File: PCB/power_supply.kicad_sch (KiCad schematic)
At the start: 7 parts, among them SW1 SW_MEC_5G

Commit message: add footprints for power supply
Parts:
- C1: footprint Capacitor_SMD:CP_Elec_6.3x7.7 -> Capacitor_SMD:CP_Elec_6.3x5.4
- D12: footprint Capacitor_SMD:C_0805_2012Metric -> Diode_SMD:D_SMA; link (none) -> https://www.tme.eu/de/details/ss14-dc/schottkydioden-smd/dc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
- L1: footprint Inductor_SMD:L_APV_APH0650 -> Inductor_SMD:L_Bourns-SRN6028; link (none) -> https://www.tme.eu/de/details/djnr6028-470-s/drosseln/ferro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
- SW1: footprint Button_Switch_THT:SW_NKK_GW12LJP -> Button_Switch_SMD:SW_Tactile_SPST_NO_Straight_CK_PTS636Sx25SMTRLFS
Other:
- note added: "Ask Jule, what battery cell holder???"
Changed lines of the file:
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@@
 	(generator_version "10.0")
 	(paper "A4")
+	(text "Ask Jule, what battery cell holder???\n"
+		(exclude_from_sim no)
+		(at 77.47 70.358 0)
+		(effects
+			(font
+				(size 1.27 1.27)
+			)
+		)
+	)
 	(text "Power Supply"
 		(exclude_from_sim no)
-		(at 156.718 59.182 0)
+		(at 162.56 55.372 0)
 		(effects
 			(font
@@
 			(width 0)
 			(type default)
-		)
-	)
-	(label "5v"
-		(at 196.85 78.74 0)
-		(effects
-			(font
-				(size 1.27 1.27)
-			)
-			(justify left bottom)
 		)
 	)
@@
 			)
 		)
-		(property "Footprint" "Capacitor_SMD:C_0805_2012Metric"
+		(property "Footprint" "Diode_SMD:D_SMA"
 			(at 158.75 95.25 0)
 			(hide yes)
@@
 		)
 		(property "Description" "Schottky diode"
+			(at 158.75 95.25 0)
+			(hide yes)
+			(show_name no)
+			(do_not_autoplace no)
+			(effects
+				(font
+					(size 1.27 1.27)
+				)
+			)
+		)
+		(property "link" "https://www.tme.eu/de/details/ss14-dc/schottkydioden-smd/dc-components/ss14/"
 			(at 158.75 95.25 0)
 			(hide yes)
@@
 			)
 		)
-		(property "Footprint" "Inductor_SMD:L_APV_APH0650"
+		(property "Footprint" "Inductor_SMD:L_Bourns-SRN6028"
 			(at 167.64 68.58 0)
 			(hide yes)
@@
 		(property "Description" "Inductor"
 			(at 167.64 68.58 0)
+			(hide yes)
+			(show_name no)
+			(do_not_autoplace no)
+			(effects
+				(font
+					(size 1.27 1.27)
+				)
+			)
+		)
+		(property "link" "https://www.tme.eu/de/details/djnr6028-470-s/drosseln/ferrocore/"
+			(at 167.64 68.58 90)
 			(hide yes)
 			(show_name no)
@@
 			)
 		)
-		(property "Datasheet" ""
+		(property "Datasheet" "https://de.aliexpress.com/item/1005009130833374.html?spm=a2g0o.order_list.order_list_main.5.39695c5fGREGny&gatewayAdapt=glo2deu"
 			(at 167.64 81.28 0)
 			(hide yes)
@@
 			)
 		)
-		(property "Footprint" "Button_Switch_THT:SW_NKK_GW12LJP"
+		(property "Footprint" "Button_Switch_SMD:SW_Tactile_SPST_NO_Straight_CK_PTS636Sx25SMTRLFS"
 			(at 133.35 63.5 0)
 			(hide yes)
@@
 			)
 		)
-		(property "Description" "MEC 5G single pole normally-open tactile switch"
+		(property "Description" "https://www.tme.eu/de/details/tact4203-319160-r/mikroschalter-tact/connfly/ds1042-03-319kkr16010/"
+			(at 133.35 68.58 0)
+			(hide yes)
+			(show_name no)
+			(do_not_autoplace no)
+			(effects
+				(font
+					(size 1.27 1.27)
+				)
+			)
+		)
+		(property "Field5" ""
 			(at 133.35 68.58 0)
 			(hide yes)
@@
 			)
 		)
-		(property "Footprint" "Capacitor_SMD:CP_Elec_6.3x7.7"
+		(property "Footprint" "Capacitor_SMD:CP_Elec_6.3x5.4"
 			(at 117.8052 81.28 0)
 			(hide yes)
@@
 			)
 		)
-		(property "Description" "Polarized capacitor"
+		(property "Description" "https://www.tme.eu/de/details/vs0j221me054000ce0/elektrolytische-kondensatoren-smd/chang/"
 			(at 116.84 77.47 0)
 			(hide yes)

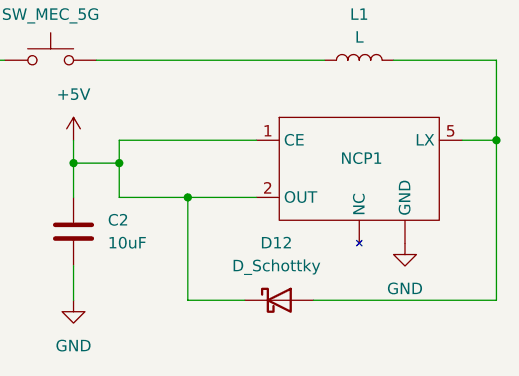
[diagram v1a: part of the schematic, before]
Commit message: update LED footprint reverse mount
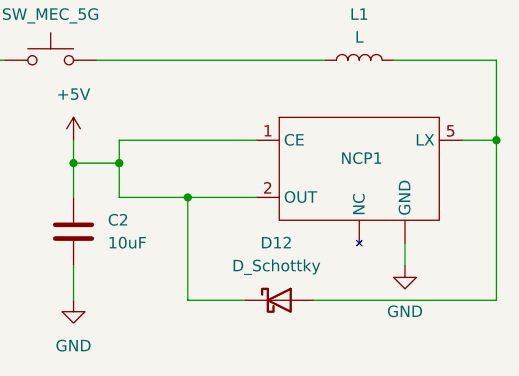
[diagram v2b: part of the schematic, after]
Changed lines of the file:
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@@
+	(wire
+		(pts
+			(xy 172.72 91.44) (xy 172.72 88.9)
+		)
+		(stroke
+			(width 0)
+			(type default)
+		)
+	)
 	(wire
 		(pts
@@
 	(symbol
 		(lib_id "power:GND")
-		(at 172.72 88.9 0)
+		(at 172.72 91.44 0)
 		(unit 1)
 		(body_style 1)
@@
 		(fields_autoplaced yes)
 		(property "Reference" "#PWR04"
-			(at 172.72 95.25 0)
+			(at 172.72 97.79 0)
 			(hide yes)
 			(show_name no)
@@
 		)
 		(property "Value" "GND"
-			(at 172.72 93.98 0)
+			(at 172.72 96.52 0)
 			(show_name no)
 			(do_not_autoplace no)
@@
 		)
 		(property "Footprint" ""
-			(at 172.72 88.9 0)
+			(at 172.72 91.44 0)
 			(hide yes)
 			(show_name no)
@@
 		)
 		(property "Datasheet" ""
-			(at 172.72 88.9 0)
+			(at 172.72 91.44 0)
 			(hide yes)
 			(show_name no)
@@
 		)
 		(property "Description" "Power symbol creates a global label with name \"GND\" , ground"
-			(at 172.72 88.9 0)
+			(at 172.72 91.44 0)
 			(hide yes)
 			(show_name no)

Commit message: component distributions
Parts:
- removed SW1: SW_MEC_5G, Button_Switch_SMD:SW_Tactile_SPST_NO_Straight_CK_PTS636Sx25SMTRLFS, symbol Switch:SW_MEC_5G
- added SW3, SW4: SW_Push, Button_Switch_SMD:SW_Push_1P1T_NO_CK_PTS125Sx73PSMTR, symbol Switch:SW_Push
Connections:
- net +3.3V: now also SW3.1, SW4.1
- net GND: now also NCP1.4 (GND); no longer NCP1. (GND)
- net at L1.1: now also SW3.2, SW4.2
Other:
- moved on the sheet: D12
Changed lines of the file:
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@@
+	)
+	(junction
+		(at 142.24 68.58)
+		(diameter 0)
+		(color 0 0 0 0)
 	)
 	(junction
@@
 	)
 	(junction
+		(at 124.46 68.58)
+		(diameter 0)
+		(color 0 0 0 0)
+	)
+	(junction
 		(at 140.97 80.01)
 		(diameter 0)
@@
 	(wire
 		(pts
+			(xy 128.27 53.34) (xy 124.46 53.34)
+		)
+		(stroke
+			(width 0)
+			(type default)
+		)
+	)
+	(wire
+		(pts
+			(xy 142.24 53.34) (xy 142.24 68.58)
+		)
+		(stroke
+			(width 0)
+			(type default)
+		)
+	)
+	(wire
+		(pts
 			(xy 135.89 83.82) (xy 135.89 80.01)
 		)
@@
 	(wire
 		(pts
-			(xy 148.59 95.25) (xy 148.59 83.82)
+			(xy 148.59 100.33) (xy 148.59 83.82)
+		)
+		(stroke
+			(width 0)
+			(type default)
+		)
+	)
+	(wire
+		(pts
+			(xy 124.46 68.58) (xy 116.84 68.58)
 		)
 		(stroke
@@
 	(wire
 		(pts
+			(xy 124.46 53.34) (xy 124.46 68.58)
+		)
+		(stroke
+			(width 0)
+			(type default)
+		)
+	)
+	(wire
+		(pts
 			(xy 182.88 77.47) (xy 179.07 77.47)
 		)
@@
 	(wire
 		(pts
-			(xy 182.88 77.47) (xy 182.88 95.25)
+			(xy 182.88 77.47) (xy 182.88 100.33)
 		)
 		(stroke
@@
 	(wire
 		(pts
-			(xy 138.43 68.58) (xy 163.83 68.58)
+			(xy 138.43 68.58) (xy 142.24 68.58)
 		)
 		(stroke
@@
 	(wire
 		(pts
-			(xy 154.94 95.25) (xy 148.59 95.25)
+			(xy 154.94 100.33) (xy 148.59 100.33)
 		)
 		(stroke
@@
 	(wire
 		(pts
-			(xy 162.56 95.25) (xy 182.88 95.25)
-		)
-		(stroke
-			(width 0)
-			(type default)
-		)
-	)
-	(wire
-		(pts
-			(xy 128.27 68.58) (xy 116.84 68.58)
+			(xy 162.56 100.33) (xy 182.88 100.33)
+		)
+		(stroke
+			(width 0)
+			(type default)
+		)
+	)
+	(wire
+		(pts
+			(xy 128.27 68.58) (xy 124.46 68.58)
+		)
+		(stroke
+			(width 0)
+			(type default)
+		)
+	)
+	(wire
+		(pts
+			(xy 142.24 68.58) (xy 163.83 68.58)
 		)
 		(stroke
@@
 		(pts
 			(xy 105.41 68.58) (xy 105.41 73.66)
+		)
+		(stroke
+			(width 0)
+			(type default)
+		)
+	)
+	(wire
+		(pts
+			(xy 138.43 53.34) (xy 142.24 53.34)
 		)
 		(stroke
@@
 	(symbol
 		(lib_id "Device:D_Schottky")
-		(at 158.75 95.25 0)
+		(at 158.75 100.33 0)
 		(unit 1)
 		(body_style 1)
@@
 		(fields_autoplaced yes)
 		(property "Reference" "D12"
-			(at 158.4325 88.9 0)
+			(at 158.4325 93.98 0)
 			(show_name no)
 			(do_not_autoplace no)
@@
 		)
 		(property "Value" "D_Schottky"
-			(at 158.4325 91.44 0)
+			(at 158.4325 96.52 0)
 			(show_name no)
 			(do_not_autoplace no)
@@
 		)
 		(property "Footprint" "Diode_SMD:D_SMA"
-			(at 158.75 95.25 0)
+			(at 158.75 100.33 0)
 			(hide yes)
 			(show_name no)
@@
 		)
 		(property "Datasheet" ""
-			(at 158.75 95.25 0)
+			(at 158.75 100.33 0)
 			(hide yes)
 			(show_name no)
@@
 		)
 		(property "Description" "Schottky diode"
-			(at 158.75 95.25 0)
+			(at 158.75 100.33 0)
 			(hide yes)
 			(show_name no)
@@
 		)
 		(property "link" "https://www.tme.eu/de/details/ss14-dc/schottkydioden-smd/dc-components/ss14/"
-			(at 158.75 95.25 0)
+			(at 158.75 100.33 0)
 			(hide yes)
 			(show_name no)
@@
 				(path "/510c3167-274e-48e8-bc0f-ce517acc7f9d/31fe11dc-c780-463d-b2c9-9ca8c0ac4f4e"
 					(reference "BT1")
+					(unit 1)
+				)
+			)
+		)
+	)
+	(symbol
+		(lib_id "Switch:SW_Push")
+		(at 133.35 68.58 0)
+		(unit 1)
+		(body_style 1)
+		(exclude_from_sim no)
+		(in_bom yes)
+		(on_board yes)
+		(in_pos_files yes)
+		(dnp no)
+		(fields_autoplaced yes)
+		(property "Reference" "SW4"
+			(at 133.35 60.96 0)
+			(show_name no)
+			(do_not_autoplace no)
+			(effects
+				(font
+					(size 1.27 1.27)
+				)
+			)
+		)
+		(property "Value" "SW_Push"
+			(at 133.35 63.5 0)
+			(show_name no)
+			(do_not_autoplace no)
+			(effects
+				(font
+					(size 1.27 1.27)
+				)
+			)
+		)
+		(property "Footprint" "Button_Switch_SMD:SW_Push_1P1T_NO_CK_PTS125Sx73PSMTR"
+			(at 133.35 63.5 0)
+			(hide yes)
+			(show_name no)
+			(do_not_autoplace no)
+			(effects
+				(font
+					(size 1.27 1.27)
+				)
+			)
+		)
+		(property "Datasheet" "https://www.apem.com/medias/download/MEC_switches_serie_MULTIMEC5G.pdf"
+			(at 133.35 63.5 0)
+			(hide yes)
+			(show_name no)
+			(do_not_autoplace no)
+			(effects
+				(font
+					(size 1.27 1.27)
+				)
+			)
+		)
+		(property "Description" "Push button switch, generic, two pins"
+			(at 133.35 68.58 0)
+			(hide yes)
+			(show_name no)
+			(do_not_autoplace no)
+			(effects
+				(font
+					(size 1.27 1.27)
+				)
+			)
+		)
+		(pin "1"
+		)
+		(pin "2"
+		)
+		(instances
+			(project "UV_badge"
+				(path "/510c3167-274e-48e8-bc0f-ce517acc7f9d/31fe11dc-c780-463d-b2c9-9ca8c0ac4f4e"
+					(reference "SW4")
 					(unit 1)
 				)
@@
 	)
 	(symbol
+		(lib_id "Switch:SW_Push")
+		(at 133.35 53.34 0)
+		(unit 1)
+		(body_style 1)
+		(exclude_from_sim no)
+		(in_bom yes)
+		(on_board yes)
+		(in_pos_files yes)
+		(dnp no)
+		(fields_autoplaced yes)
+		(property "Reference" "SW3"
+			(at 133.35 45.72 0)
+			(show_name no)
+			(do_not_autoplace no)
+			(effects
+				(font
+					(size 1.27 1.27)
+				)
+			)
+		)
+		(property "Value" "SW_Push"
+			(at 133.35 48.26 0)
+			(show_name no)
+			(do_not_autoplace no)
+			(effects
+				(font
+					(size 1.27 1.27)
+				)
+			)
+		)
+		(property "Footprint" "Button_Switch_SMD:SW_Push_1P1T_NO_CK_PTS125Sx73PSMTR"
+			(at 133.35 48.26 0)
+			(hide yes)
+			(show_name no)
+			(do_not_autoplace no)
+			(effects
+				(font
+					(size 1.27 1.27)
+				)
+			)
+		)
+		(property "Datasheet" "https://www.apem.com/medias/download/MEC_switches_serie_MULTIMEC5G.pdf"
+			(at 133.35 48.26 0)
+			(hide yes)
+			(show_name no)
+			(do_not_autoplace no)
+			(effects
+				(font
+					(size 1.27 1.27)
+				)
+			)
+		)
+		(property "Description" "Push button switch, generic, two pins"
+			(at 133.35 53.34 0)
+			(hide yes)
+			(show_name no)
+			(do_not_autoplace no)
+			(effects
+				(font
+					(size 1.27 1.27)
+				)
+			)
+		)
+		(pin "1"
+		)
+		(pin "2"
+		)
+		(instances
+			(project "UV_badge"
+				(path "/510c3167-274e-48e8-bc0f-ce517acc7f9d/31fe11dc-c780-463d-b2c9-9ca8c0ac4f4e"
+					(reference "SW3")
+					(unit 1)
+				)
+			)
+		)
+	)
+	(symbol
 		(lib_id "custom:NCP1402")
 		(at 167.64 81.28 0)
@@
 			)
 		)
-		(pin ""
-		)
-		(pin ""
+		(pin "3"
+		)
+		(pin "4"
 		)
 		(pin "1"
@@
 					(unit 1)
 				)
-			)
-		)
-	)
-	(symbol
-		(lib_id "Switch:SW_MEC_5G")
-		(at 133.35 68.58 0)
-		(unit 1)
-		(body_style 1)
-		(exclude_from_sim no)
-		(in_bom yes)
-		(on_board yes)
-		(in_pos_files yes)
-		(dnp no)
-		(fields_autoplaced yes)
-		(property "Reference" "SW1"
-			(at 133.35 60.96 0)
-			(show_name no)
-			(do_not_autoplace no)
-			(effects
-				(font
-					(size 1.27 1.27)
-				)
-			)
-		)
-		(property "Value" "SW_MEC_5G"
-			(at 133.35 63.5 0)
-			(show_name no)
-			(do_not_autoplace no)
-			(effects
-				(font
-					(size 1.27 1.27)
-				)
-			)
-		)
-		(property "Footprint" "Button_Switch_SMD:SW_Tactile_SPST_NO_Straight_CK_PTS636Sx25SMTRLFS"
-			(at 133.35 63.5 0)
-			(hide yes)
-			(show_name no)
-			(do_not_autoplace no)
-			(effects
-				(font
-					(size 1.27 1.27)
-				)
-			)
-		)
-		(property "Datasheet" "https://www.apem.com/medias/download/MEC_switches_serie_MULTIMEC5G.pdf"
-			(at 133.35 63.5 0)
-			(hide yes)
-			(show_name no)
-			(do_not_autoplace no)
-			(effects
-				(font
-					(size 1.27 1.27)
-				)
-			)
-		)
-		(property "Description" "https://www.tme.eu/de/details/tact4203-319160-r/mikroschalter-tact/connfly/ds1042-03-319kkr16010/"
-			(at 133.35 68.58 0)
-			(hide yes)
-			(show_name no)
-			(do_not_autoplace no)
-			(effects
-				(font
-					(size 1.27 1.27)
-				)
-			)
-		)
-		(property "Field5" ""
-			(at 133.35 68.58 0)
-			(hide yes)
-			(show_name no)
-			(do_not_autoplace no)
-			(effects
-				(font
-					(size 1.27 1.27)
-				)
-			)
-		)
-		(pin "2"
-		)
-		(pin "1"
-		)
-		(pin "4"
-		)
-		(pin "3"
-		)
-		(instances
-			(project "UV_badge"
-				(path "/510c3167-274e-48e8-bc0f-ce517acc7f9d/31fe11dc-c780-463d-b2c9-9ca8c0ac4f4e"
-					(reference "SW1")
-					(unit 1)
-				)
